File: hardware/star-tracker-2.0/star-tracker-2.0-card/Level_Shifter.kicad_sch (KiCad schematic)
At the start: 48 parts, among them U5 SN74LVC8T245MPWREPPW24-M, U6 CLVCH16T245MDGGREP, U8 TLV70028QDDCRQ1, U9 TCA9509DGKRDGK8-M

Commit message: Routine Push
Updated schematic and layout. about 60% done with routing.
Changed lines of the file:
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@@
+	(wire
+		(pts
+			(xy 0.0762 0.0762) (xy 82.6262 0.0762)
+		)
+		(stroke
+			(width 0)
+			(type default)
+		)
+	)
 	(wire
 		(pts
@@
 		)
 	)
+	(wire
+		(pts
+			(xy 1.3462 1.3462) (xy 83.8962 1.3462)
+		)
+		(stroke
+			(width 0)
+			(type default)
+		)
+	)

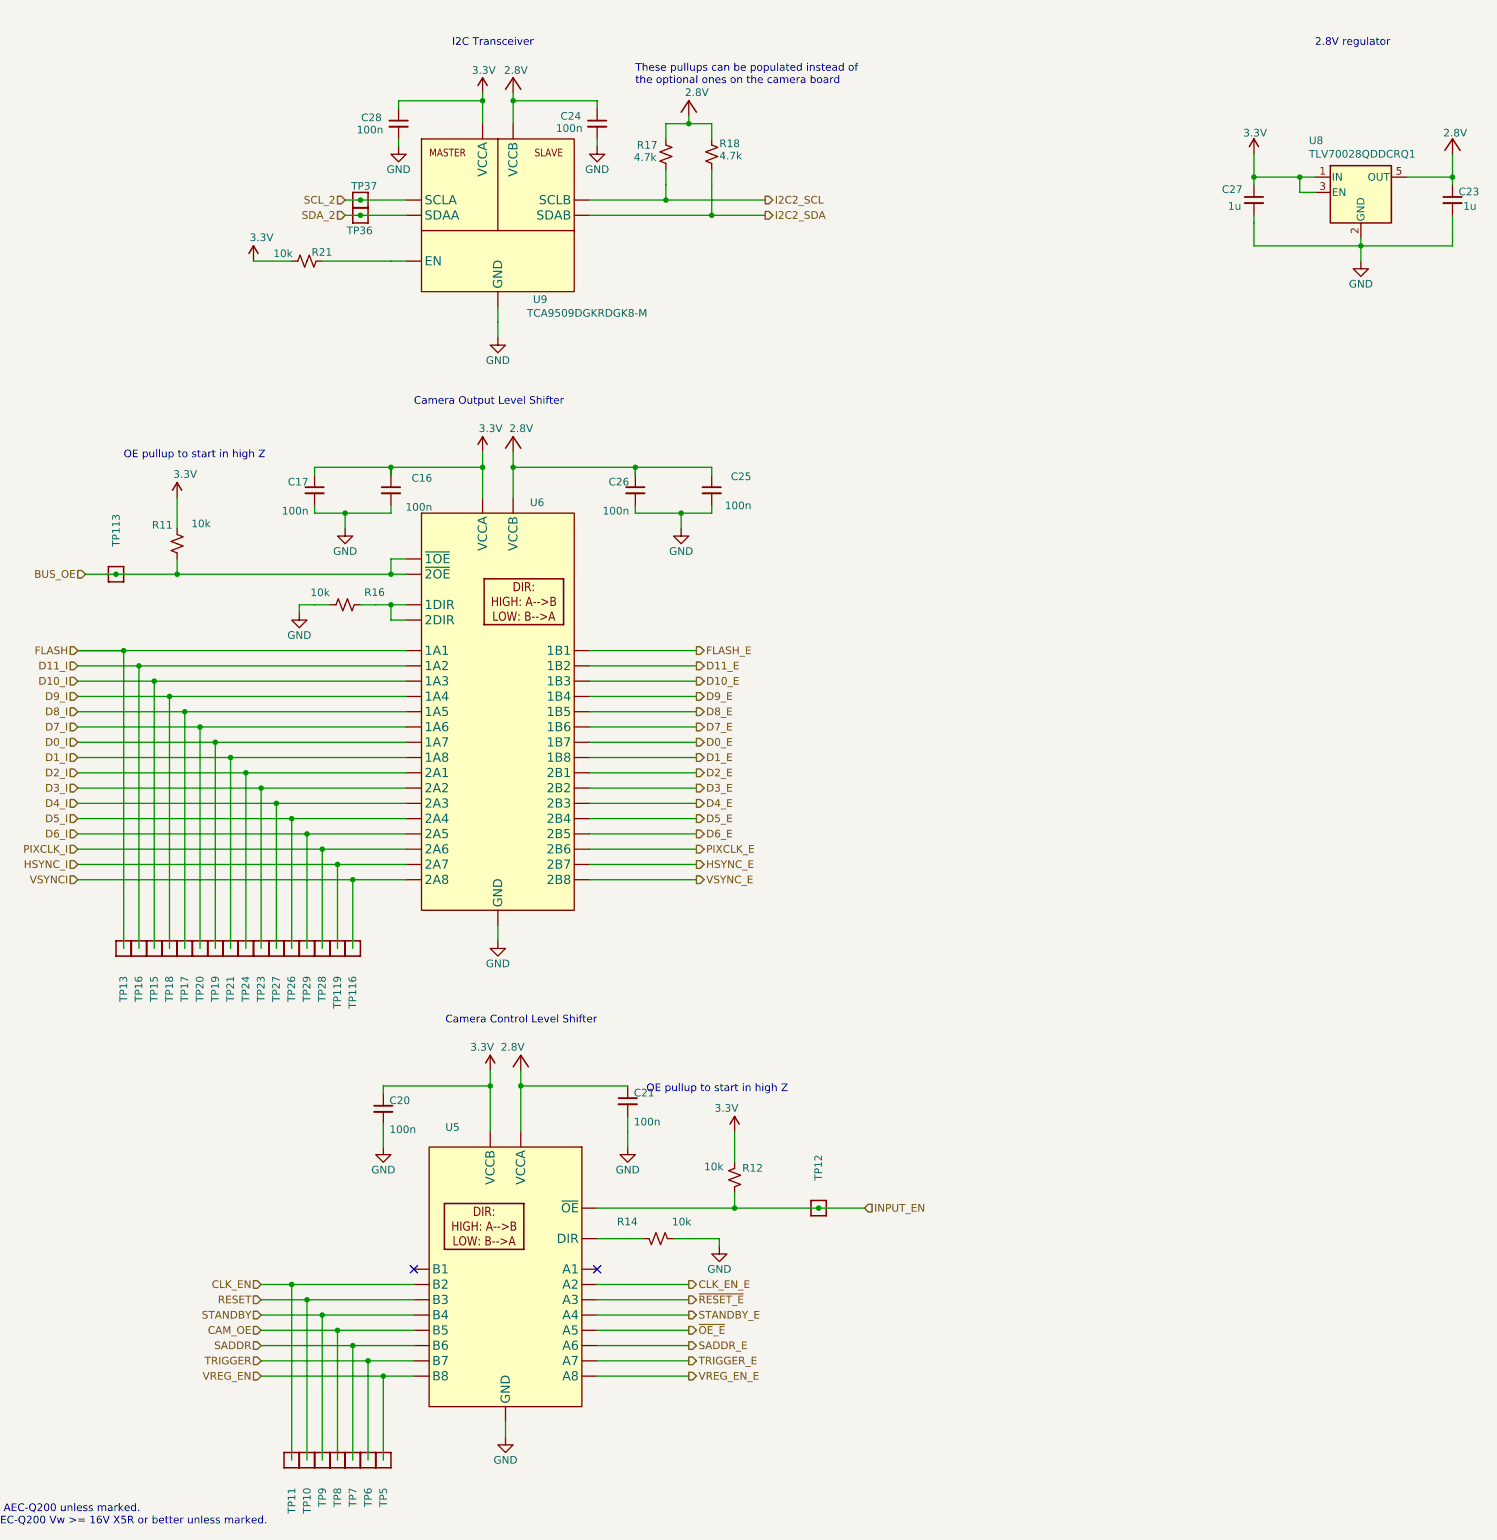
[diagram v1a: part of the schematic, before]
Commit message: Star tracker board update
Added 3d models to footprints, reannotated component designators
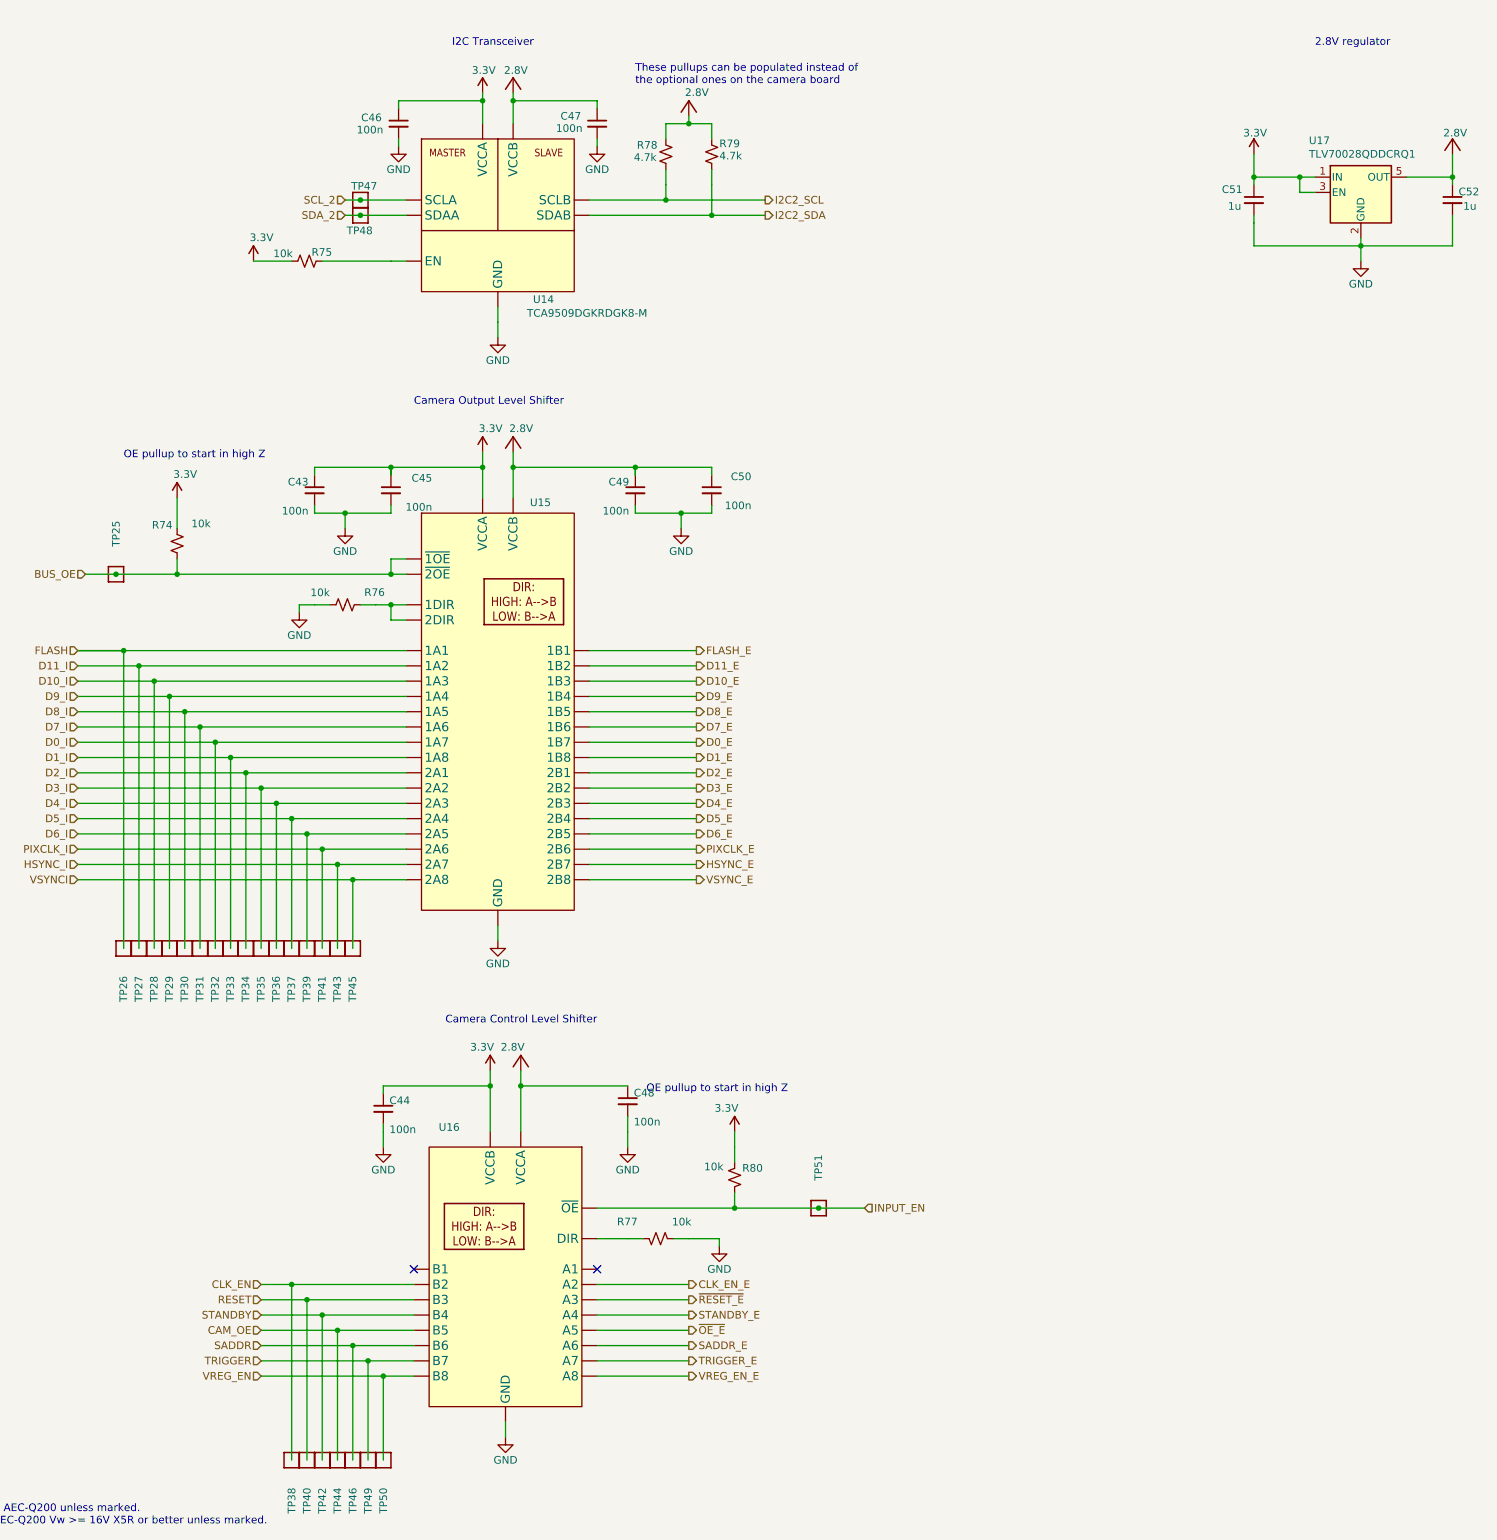
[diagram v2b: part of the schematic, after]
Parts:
- renumbered C17 to C43, C20 to C44, C16 to C45, C28 to C46, C24 to C47, C21 to C48, C26 to C49, C25 to C50, C27 to C51, C23 to C52, R11 to R74, R21 to R75, R16 to R76, R14 to R77, R17 to R78, R18 to R79, R12 to R80, TP113 to TP25, TP13 to TP26, TP16 to TP27, TP15 to TP28, TP18 to TP29, TP17 to TP30, TP20 to TP31, TP19 to TP32, TP21 to TP33, TP24 to TP34, TP23 to TP35, TP27 to TP36, TP26 to TP37, TP11 to TP38, TP29 to TP39, TP10 to TP40, TP28 to TP41, TP9 to TP42, TP119 to TP43, TP8 to TP44, TP116 to TP45, TP7 to TP46, TP37 to TP47, TP36 to TP48, TP6 to TP49, TP5 to TP50, TP12 to TP51, U9 to U14, U6 to U15, U5 to U16, U8 to U17

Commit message: Added extra Testpoints
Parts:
- added TP53: TEST-POINT, star-tracker-card:2MM-TEST-POINT, symbol star-tracker-card-eagle-import:TEST-POINT
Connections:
- net 2.8V: now also TP53.1
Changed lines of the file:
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@@
 	)
 	(junction
+		(at 375.92 39.37)
+		(diameter 0)
+		(color 0 0 0 0)
+	)
+	(junction
 		(at 154.94 120.65)
 		(diameter 0)
@@
 	(wire
 		(pts
-			(xy 375.92 41.91) (xy 375.92 38.1)
+			(xy 375.92 41.91) (xy 375.92 39.37)
 		)
 		(stroke
@@
 	(wire
 		(pts
+			(xy 375.92 39.37) (xy 375.92 38.1)
+		)
+		(stroke
+			(width 0.1524)
+			(type solid)
+		)
+	)
+	(wire
+		(pts
 			(xy 256.54 210.82) (xy 256.54 213.36)
 		)
@@
 					(unit 1)
 				)
+			)
+		)
+	)
+	(symbol
+		(lib_id "star-tracker-card-eagle-import:TEST-POINT")
+		(at 375.92 39.37 180)
+		(unit 1)
+		(body_style 1)
+		(exclude_from_sim no)
+		(in_bom no)
+		(on_board yes)
+		(in_pos_files yes)
+		(dnp no)
+		(property "Reference" "TP53"
+			(at 382.524 38.862 0)
+			(show_name no)
+			(do_not_autoplace no)
+			(effects
+				(font
+					(size 1.27 1.27)
+				)
+				(justify left bottom)
+			)
+		)
+		(property "Value" "TEST-POINT"
+			(at 375.92 39.37 0)
+			(hide yes)
+			(show_name no)
+			(do_not_autoplace no)
+			(effects
+				(font
+					(size 1.27 1.27)
+				)
+			)
+		)
+		(property "Footprint" "star-tracker-card:2MM-TEST-POINT"
+			(at 375.92 39.37 0)
+			(hide yes)
+			(show_name no)
+			(do_not_autoplace no)
+			(effects
+				(font
+					(size 1.27 1.27)
+				)
+			)
+		)
+		(property "Datasheet" ""
+			(at 375.92 39.37 0)
+			(hide yes)
+			(show_name no)
+			(do_not_autoplace no)
+			(effects
+				(font
+					(size 1.27 1.27)
+				)
+			)
+		)
+		(property "Description" ""
+			(at 375.92 39.37 0)
+			(hide yes)
+			(show_name no)
+			(do_not_autoplace no)
+			(effects
+				(font
+					(size 1.27 1.27)
+				)
+			)
+		)
+		(pin "1"
+		)
+		(instances
+			(project "star-tracker-card"
+				(path "/324e9eb5-7420-4b7e-862c-cc20bb28618a/9edd79c7-1f35-42ab-883b-4f04e19f8786"
+					(reference "TP53")
+					(unit 1)
+				)
